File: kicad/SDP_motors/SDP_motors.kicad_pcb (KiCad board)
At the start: 2 copper layers, 69 parts, among them J1 Conn_01x04, J2 Conn_01x04, J3 Conn_01x04, J4 Conn_01x04, J5 Conn_01x04, J6 Conn_01x04, J7 Conn_01x02, J8 Conn_01x02, J9 Conn_01x02, Q1 IRLZ44N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

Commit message: Added proximity sensor headers
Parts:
- added H1: MountingHole_Pad, MountingHole:MountingHole_3.2mm_M3_Pad, F.Cu at (172.2, 43.5)
- added H2: MountingHole_Pad, MountingHole:MountingHole_3.2mm_M3_Pad, F.Cu at (83.2, 43.5)
- added H3: MountingHole_Pad, MountingHole:MountingHole_3.2mm_M3_Pad, F.Cu at (83.2, 132.5)
- added H4: MountingHole_Pad, MountingHole:MountingHole_3.2mm_M3_Pad, F.Cu at (172.2, 132.5)
- added J10: MOTOR, Connector_PinSocket_2.54mm:PinSocket_2x08_P2.54mm_Vertical, F.Cu at (81.8, 96.4)
- added TP1: TestPoint_Small, TestPoint:TestPoint_Pad_D2.0mm, F.Cu at (145.5, 106.6)
- added TP2: TestPoint_Small, TestPoint:TestPoint_Pad_D2.0mm, F.Cu at (141.4, 106.4)
- added TP3: TestPoint_Small, TestPoint:TestPoint_Pad_D2.0mm, F.Cu at (141.4, 102.4)
- added TP4: TestPoint_Small, TestPoint:TestPoint_Pad_D2.0mm, F.Cu at (145.4, 102.4)
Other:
- board outline added: 98 x 98 mm

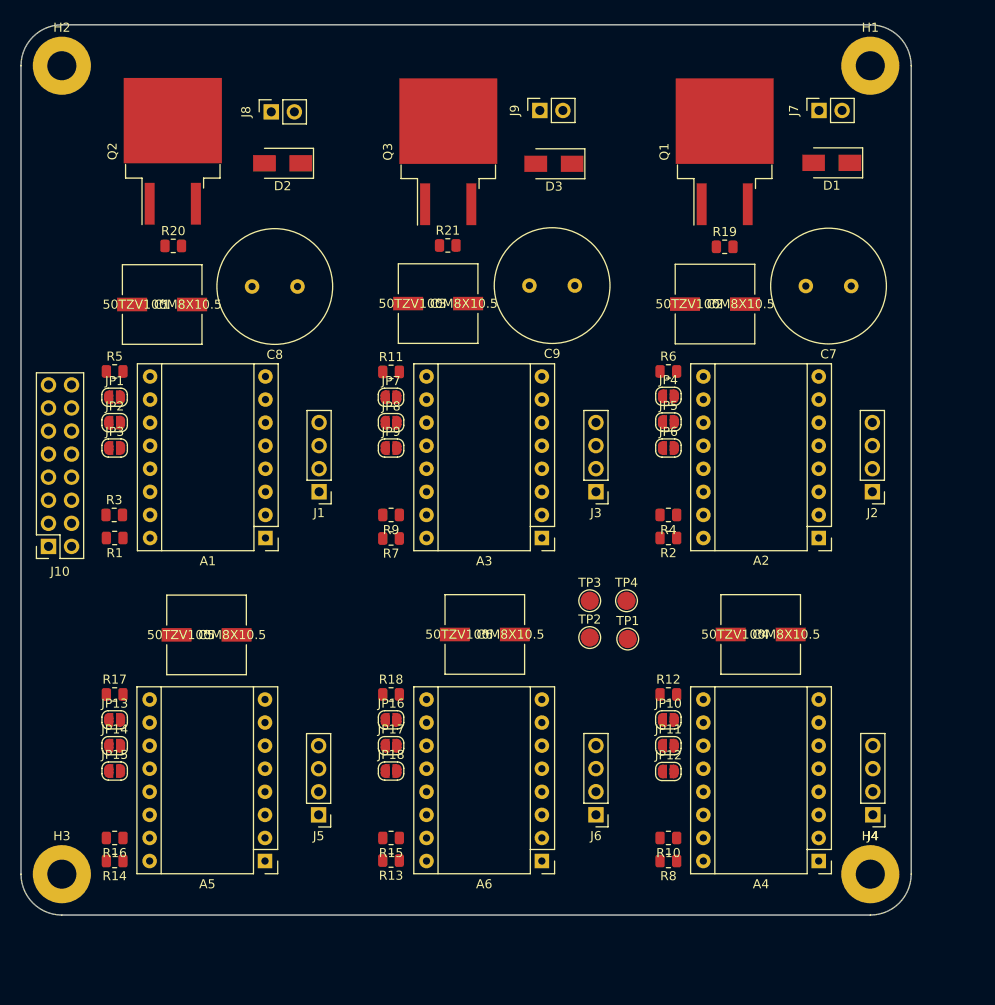
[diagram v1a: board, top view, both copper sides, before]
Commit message: Motor PCB layout
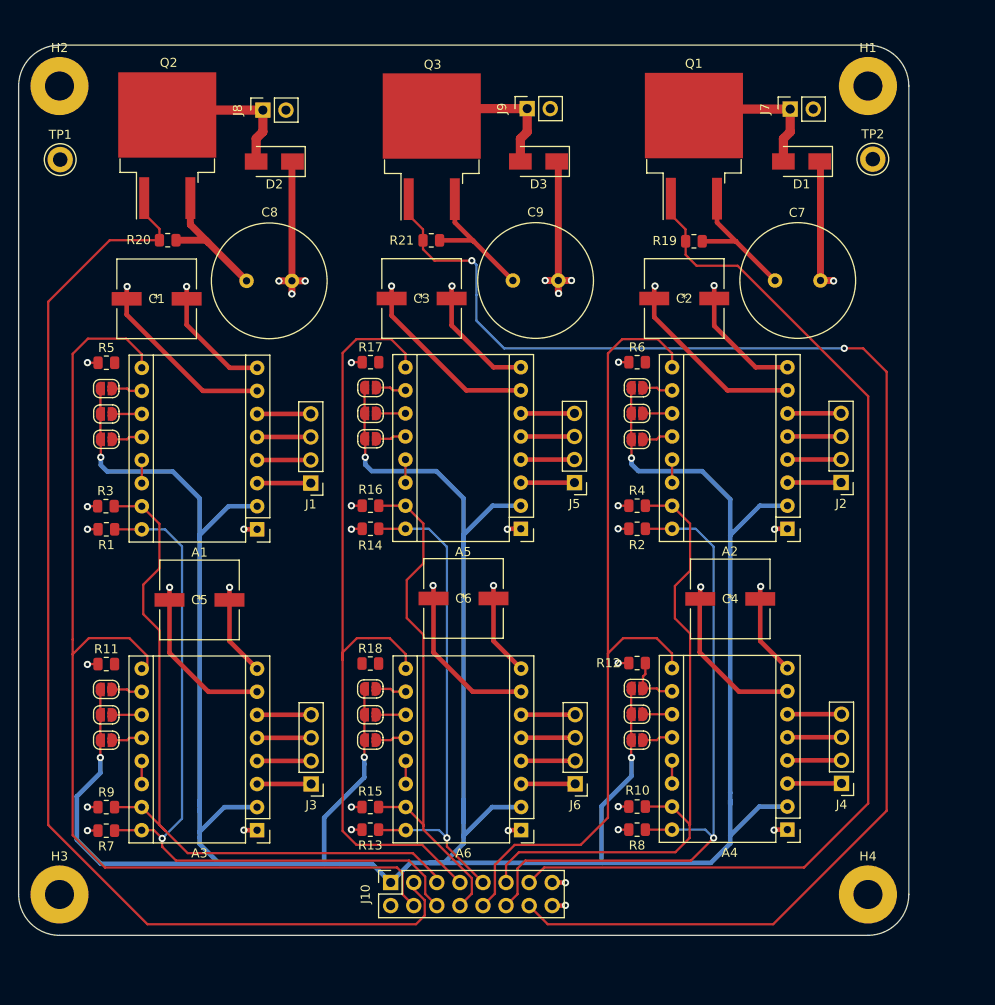
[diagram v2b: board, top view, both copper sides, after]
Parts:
- removed the TP1 at (145.5, 106.6)
- removed the TP2 at (141.4, 106.4)
- TP1: renamed from TP3; footprint TestPoint:TestPoint_Pad_D2.0mm -> TestPoint:TestPoint_Keystone_5005-5009_Compact
- TP2: renamed from TP4; footprint TestPoint:TestPoint_Pad_D2.0mm -> TestPoint:TestPoint_Keystone_5005-5009_Compact
- moved TP1 75.9 mm to (83.1, 53.8)
- moved TP2 55.7 mm to (172.5, 53.7)
- moved J10 52.8 mm to (119.4, 133.4), turned to 90 degrees
- moved A5 46.2 mm to (133.8, 94.4)
- moved JP13 46.2 mm to (117.2, 78.9)
- moved JP15 46.2 mm to (117.2, 84.5)
- moved R14 46.2 mm to (117.2, 94.4)
- moved R17 46.2 mm to (117.2, 76.1)
- moved JP14 46.2 mm to (117.2, 81.7)
- moved J5 46.2 mm to (139.7, 89.4)
- moved R16 46.2 mm to (117.2, 91.9)
- moved A3 44.9 mm to (104.7, 127.6)
- moved JP7 44.9 mm to (88.1, 112.1)
- moved J3 44.9 mm to (110.7, 122.5)
- moved JP8 44.9 mm to (88.1, 114.9)
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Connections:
- H1 pad 1: GND -> unconnected-(H1-Pad1)
- H2 pad 1: GND -> unconnected-(H2-Pad1)
- H3 pad 1: GND -> unconnected-(H3-Pad1)
- H4 pad 1: GND -> unconnected-(H4-Pad1)
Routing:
- net +3V3: track 0.00 -> 371.6 mm, vias 0 -> 6
- net GND: track 0.00 -> 197.0 mm, vias 0 -> 30
- net P88_MTR2: track 0.00 -> 160.1 mm, vias 0 -> 2
- net P72_FAN: track 0.00 -> 128.5 mm
- net +12V: track 0.00 -> 124.3 mm, vias 0 -> 14
- net P87_MTR1: track 0.00 -> 119.2 mm
- net P76_EN: track 0.00 -> 116.7 mm
- net P82_EN: track 0.00 -> 91.8 mm
- net P79_EN: track 0.00 -> 88.3 mm
- net P78_DIR: track 0.00 -> 81.8 mm, vias 0 -> 1
- net P77_STEP: track 0.00 -> 80.6 mm
- net P84_DIR: track 0.00 -> 75.9 mm, vias 0 -> 1
- net P83_STEP: track 0.00 -> 70.9 mm
- net P80_STEP: track 0.00 -> 57.9 mm
- net P81_DIR: track 0.00 -> 54.8 mm, vias 0 -> 1
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- added copper zone on In2.Cu, net +12V
- added copper zone on In1.Cu, net GND
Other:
- copper layers 2 -> 4

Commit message: Controller and motor PCB silkscreen and final layout
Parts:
- moved J6 9.32 mm to (147.2, 128.1)
- moved A2 9.32 mm to (170.6, 100.0)
- moved D3 9.32 mm to (143.2, 59.6)
- moved H1 9.32 mm to (179.4, 51.3)
- moved J4 9.32 mm to (176.5, 128.1)
- moved J9 9.32 mm to (141.9, 53.8)
- moved JP10 9.32 mm to (154.0, 117.6)
- moved JP11 9.32 mm to (154.0, 120.5)
- moved JP12 9.32 mm to (154.0, 123.3)
- moved JP4 9.32 mm to (154.0, 84.5)
- moved JP5 9.32 mm to (154.0, 87.3)
- moved R12 9.32 mm to (154.0, 114.8)
- moved R8 9.32 mm to (154.0, 133.2)
- moved J10 9.32 mm to (126.9, 139.0)
- moved TP2 9.32 mm to (180.0, 59.4)
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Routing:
- net Net-(A1-Pad10): track 3.37 -> 6.33 mm
- net Net-(A2-Pad10): track 3.33 -> 6.26 mm
- net Net-(A3-Pad10): track 3.37 -> 6.27 mm
- net Net-(A6-Pad10): track 3.38 -> 6.28 mm
- net Net-(A5-Pad10): track 3.33 -> 6.23 mm
- net +3V3: track 371.6 -> 368.7 mm
- net P72_FAN: track 128.5 -> 129.6 mm
- net GND: track 197.0 -> 196.6 mm, vias 30 -> 37
- added copper zone on B.Cu, net GND
- added copper zone on F.Cu, net GND

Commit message: Final PCB layout changes
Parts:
- J7, J8, J9: footprint Connector_PinSocket_2.54mm:PinSocket_1x02_P2.54mm_Vertical -> TerminalBlock_Phoenix:TerminalBlock_Phoenix_PT-1,5-2-5.0-H_1x02_P5.00mm_Horizontal
- moved TP2 74.3 mm to (179.4, 133.7)
- moved J8 2.41 mm to (114.7, 52.4), turned to 180 degrees
- moved J9 2.26 mm to (143.7, 52.4), turned to 180 degrees
- moved J7 2.22 mm to (172.6, 52.4), turned to 180 degrees
- moved D2 2.04 mm to (112.1, 60.2)
- moved D1 1.92 mm to (170.3, 60.2)
- moved D3 1.89 mm to (141.4, 60.2)
- moved A6 1.83 mm to (139.4, 133.3)
- moved R10 1.83 mm to (152.2, 130.7)
- moved R7 1.83 mm to (93.7, 133.4)
- moved R9 1.83 mm to (93.7, 130.8)
- moved C2 1.83 mm to (157.4, 74.8)
- moved C3 1.83 mm to (128.5, 74.8)
- moved C7 1.83 mm to (172.4, 72.8)
- moved C9 1.83 mm to (143.5, 72.8)
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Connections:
- J7 pad 1: Net-(D1-Pad2) -> +12V
- J7 pad 2: +12V -> Net-(D1-Pad2)
- J8 pad 1: Net-(D2-Pad2) -> +12V
- J8 pad 2: +12V -> Net-(D2-Pad2)
- J9 pad 1: Net-(D3-Pad2) -> +12V
- J9 pad 2: +12V -> Net-(D3-Pad2)
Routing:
- net +12V: track 124.2 -> 113.8 mm, vias 14 -> 7
- net GND: track 196.6 -> 202.0 mm, vias 37 -> 38
- net P84_DIR: track 75.9 -> 72.9 mm
- net P88_MTR2: track 159.9 -> 157.7 mm
- net Net-(D2-Pad2): track 16.7 -> 15.1 mm
- net P72_FAN: track 129.6 -> 128.2 mm
- net P77_STEP: track 80.6 -> 82.0 mm
- net P83_STEP: track 70.9 -> 69.5 mm
- net P82_EN: track 91.8 -> 90.5 mm
- net P87_MTR1: track 119.2 -> 117.8 mm
- net Net-(D3-Pad2): track 17.0 -> 18.2 mm
- net Net-(D1-Pad2): track 17.0 -> 18.1 mm
- net P80_STEP: track 57.9 -> 58.9 mm
- net P79_EN: track 88.3 -> 89.3 mm
- net P78_DIR: track 81.8 -> 82.7 mm
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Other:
- board text added: "+"
- board text added: "GND"
- board text added: "JLCJLCJLCJLC"
